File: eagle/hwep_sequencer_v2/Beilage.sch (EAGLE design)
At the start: 145 parts, among them X1 ESP32-DEVKIT-C

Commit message: final commit before testing
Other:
- note added: "Index/Cursor"
- note removed: "Select"
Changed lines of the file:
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@@
 <wire x1="5.08" y1="48.26" x2="5.08" y2="154.94" width="0.1524" layer="97" style="dashdot"/>
 <text x="93.98" y="261.62" size="1.778" layer="97" font="vector" align="bottom-center">Key Register Bar Interface</text>
-<text x="48.26" y="149.86" size="1.778" layer="97" font="vector" align="bottom-center">Select</text>
+<text x="48.26" y="149.86" size="1.778" layer="97" font="vector" align="bottom-center">Index/Cursor</text>
 <text x="142.24" y="149.86" size="1.778" layer="97" font="vector" align="bottom-center">Enable</text>
 <wire x1="83.82" y1="144.78" x2="83.82" y2="147.32" width="0.1524" layer="97"/>

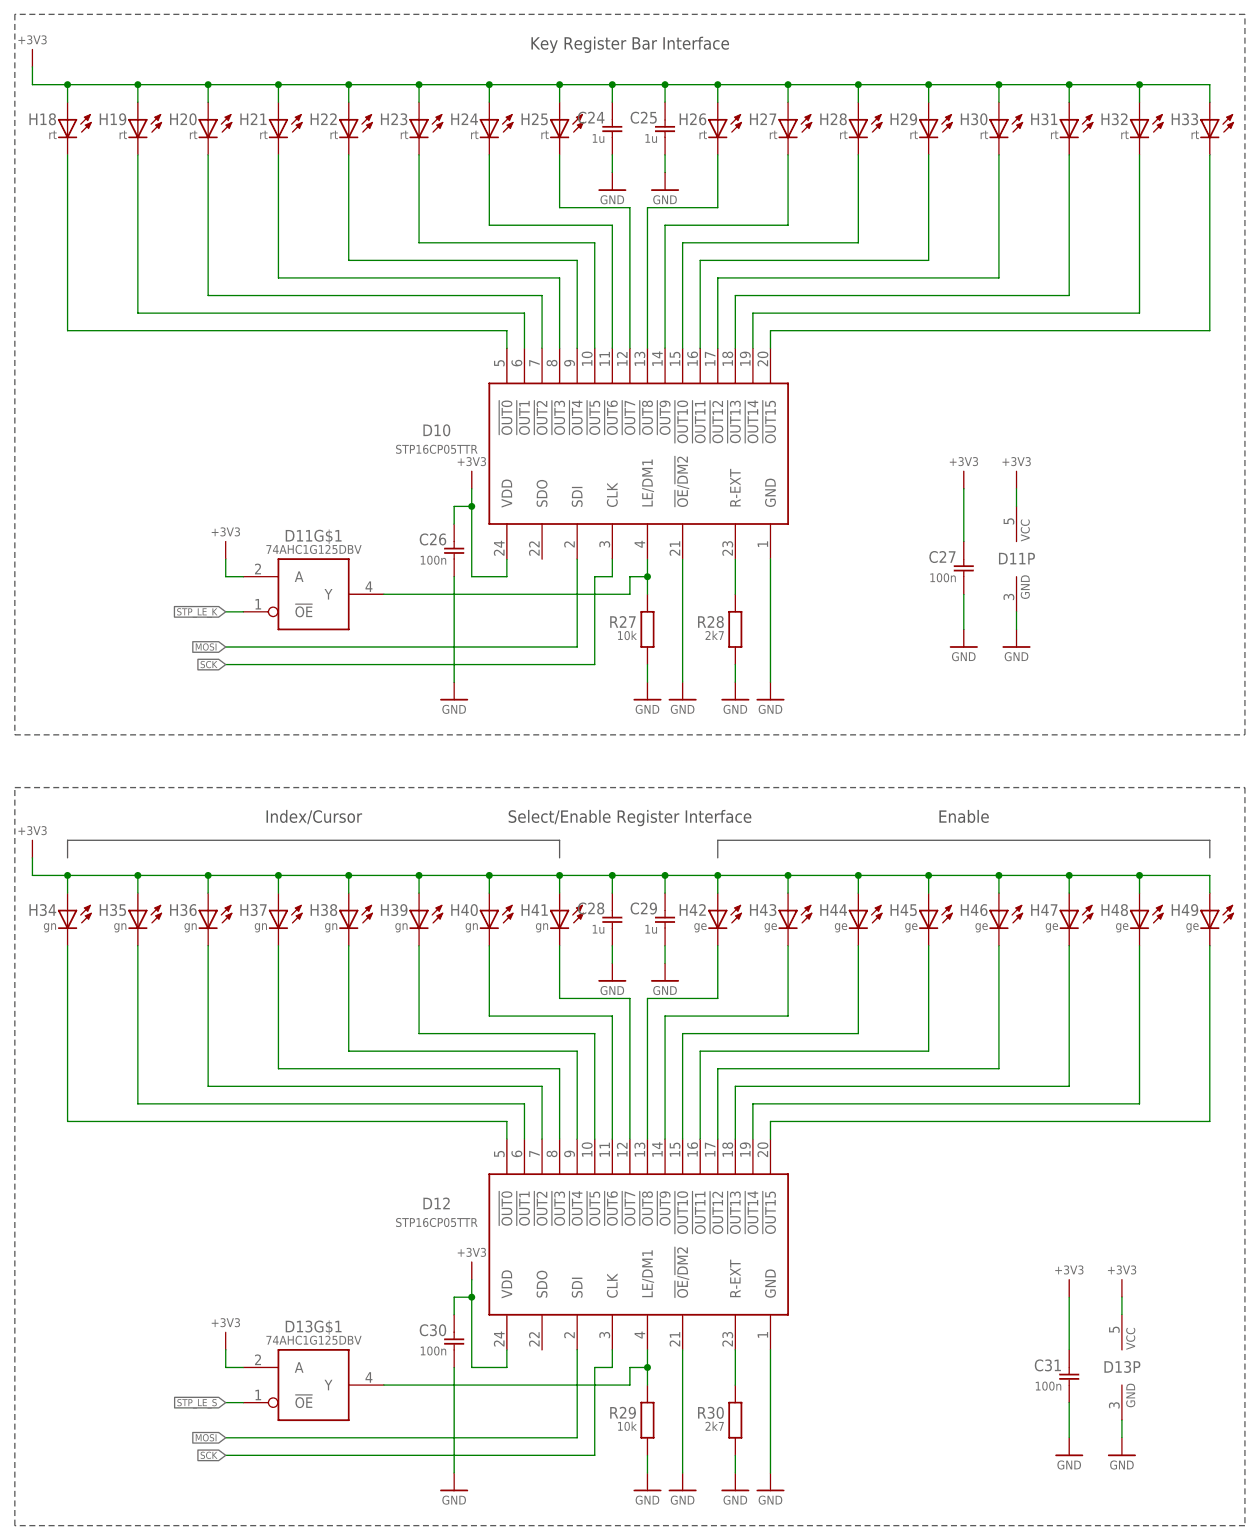
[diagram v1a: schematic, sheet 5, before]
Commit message: removed key register visualisation
bloat feature
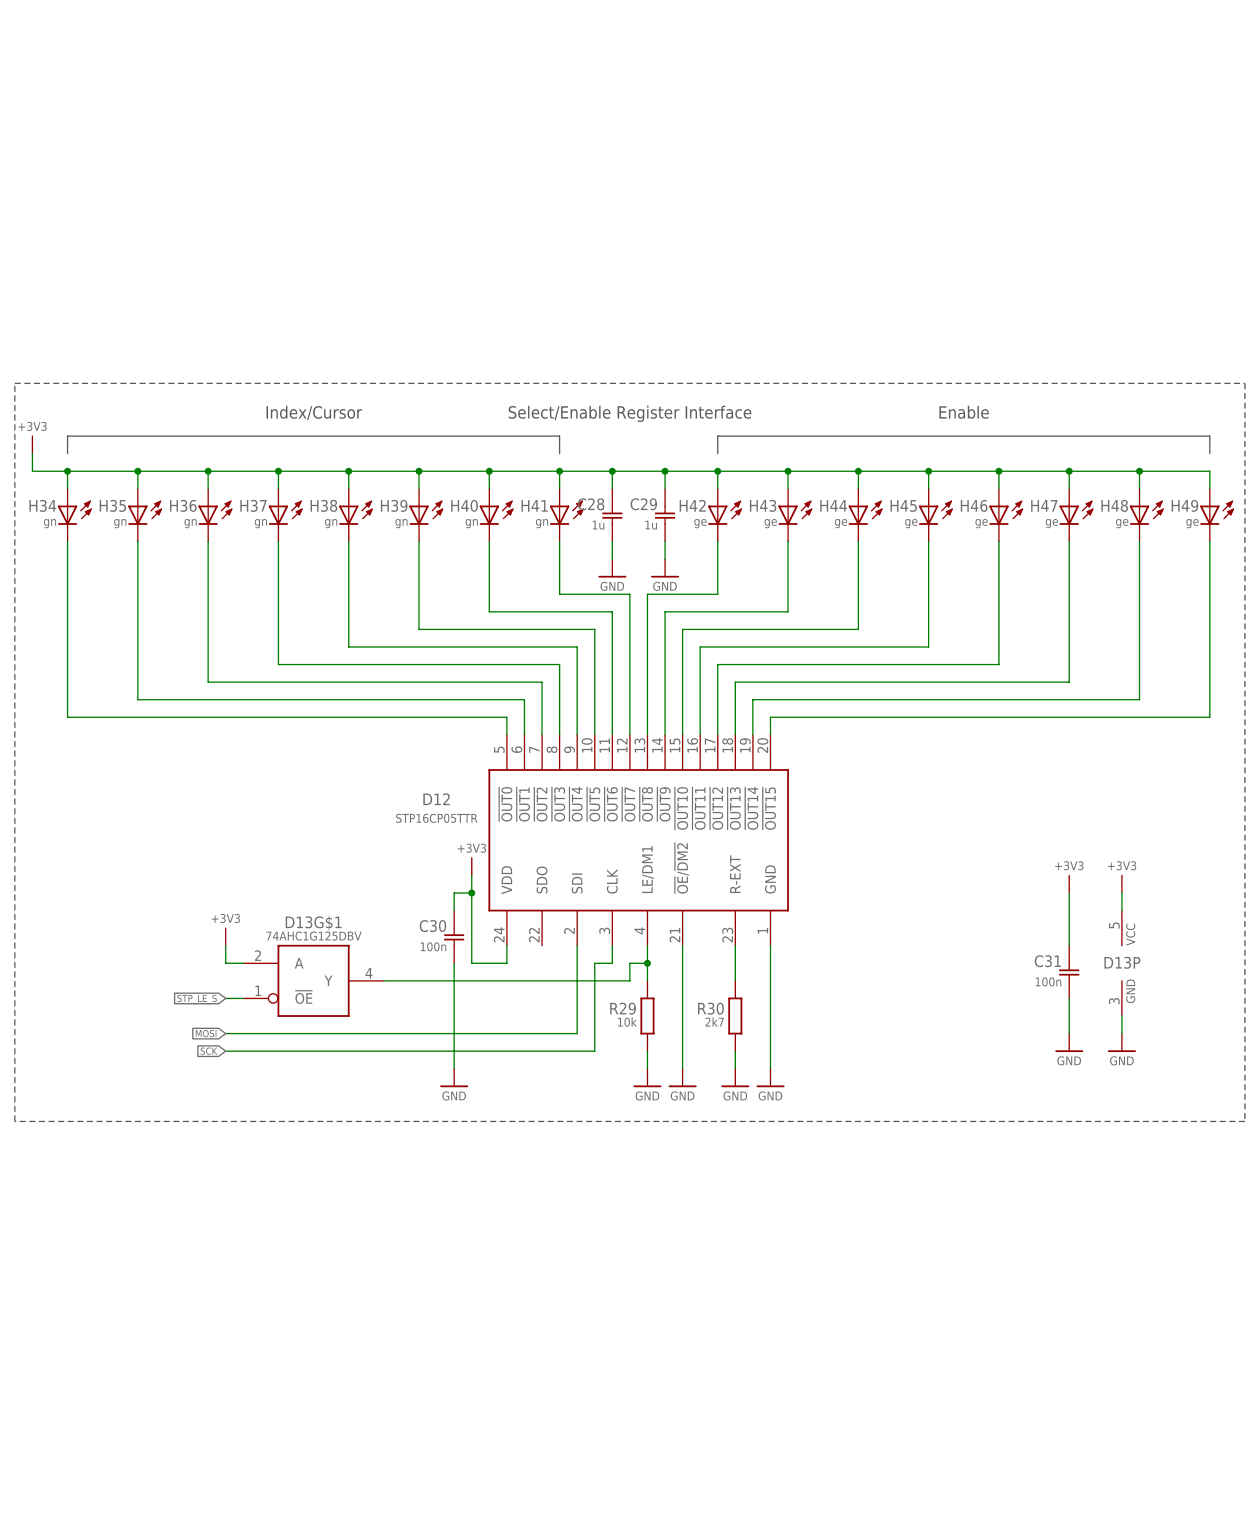
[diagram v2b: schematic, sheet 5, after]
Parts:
- removed C24, C25: 1u, rcl_GruS:C-EUC0805
- removed C26, C27: 100n, rcl_GruS:C-EUC0805
- removed D10: STP16CP05TTR, ic_GruS:STP16CP05TTR
- removed D11: 74AHC1G125DBV, 74xx_GruS:74AHC1G125DBV
- removed H18, H19, H20, H21, H22, H23, H24, H25, H26, H27, H28, H29, H30, H31, H32, H33: rt, led_GruS:LEDCHIPLED_1206
- removed R27: 10k, rcl_GruS:R-EUSR0805
- removed R28: 2k7, rcl_GruS:R-EUSR0805
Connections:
- net CLRR renamed RKR
- removed net N$10: D10.!OUT0, H18.C
- removed net N$11: D10.!OUT1, H19.C
- removed net N$12: D10.!OUT2, H20.C
- removed net N$13: D10.!OUT3, H21.C
- removed net N$20: D10.!OUT4, H22.C
- removed net N$21: D10.!OUT5, H23.C
- removed net N$22: D10.!OUT6, H24.C
- removed net N$23: D10.!OUT7, H25.C
- removed net N$24: D10.R-EXT, R28.2
- removed net N$25: D10.!OUT8, H26.C
- removed net N$26: D10.!OUT9, H27.C
- removed net N$27: D10.!OUT10, H28.C
- removed net N$28: D10.!OUT11, H29.C
- removed net N$29: D10.!OUT12, H30.C
- removed net N$30: D10.!OUT13, H31.C
- removed net N$31: D10.!OUT14, H32.C
- removed net N$32: D10.!OUT15, H33.C
- removed net N$66: D10.LE/DM1, D11G$1.Y, R27.2
- net +3V3: no longer C24.1, C25.1, C26.1, C27.1, D10.VDD, D11G$1.A, D11P.VCC, H18.A, H19.A, H20.A, H21.A, H22.A, H23.A, H24.A, H25.A, H26.A, H27.A, H28.A, H29.A, H30.A, H31.A, H32.A, H33.A
- net GND: no longer C24.2, C25.2, C26.2, C27.2, D10.!OE!/!DM2, D10.GND, D11P.GND, R27.1, R28.1
- net MOSI: no longer D10.SDI
- net SCK: no longer D10.CLK
- net STP_LE_K: no longer D11G$1.!OE
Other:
- note removed: "Key Register Bar Interface"
- moved on the sheet: C28, C29, C30, C31, D12, D13G$1, D13P, H34, H35, H36, H37, H38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

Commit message: upd doku
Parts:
- C4: CATEGORY (none) -> 2
- X3, X4: CATEGORY (none) -> 18
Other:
- note removed: "Prescaler 4-bit encoded data priority on BPM Divider Inputs"
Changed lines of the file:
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@@
 <attributes>
 <attribute name="ABTEILUNG" value="Technische Informatik"/>
-<attribute name="BEARBEITER" value="Simon Grundner"/>
-<attribute name="DATUM" value="2021//"/>
+<attribute name="BEARBEITER" value="Ihninger, Grundner"/>
+<attribute name="DATUM" value="07/02/2022"/>
 <attribute name="DOKUMENTART" value="Schaltplan"/>
 <attribute name="GEZ" value="GruS"/>
@@
 <part name="GND11" library="supply_GruS" library_urn="urn:adsk.eagle:library:13579815" deviceset="AGND" device=""/>
 <part name="GND12" library="supply_GruS" library_urn="urn:adsk.eagle:library:13579815" deviceset="AGND" device=""/>
-<part name="X4" library="con_GruS" library_urn="urn:adsk.eagle:library:13569504" deviceset="JUMPSMD1FACH-1" device="" package3d_urn="urn:adsk.eagle:package:33704775/1"/>
-<part name="X3" library="con_GruS" library_urn="urn:adsk.eagle:library:13569504" deviceset="JUMPSMD1FACH-1" device="" package3d_urn="urn:adsk.eagle:package:33704775/1"/>
+<part name="X4" library="con_GruS" library_urn="urn:adsk.eagle:library:13569504" deviceset="JUMPSMD1FACH-1" device="" package3d_urn="urn:adsk.eagle:package:33704775/1">
+<attribute name="CATEGORY" value="18"/>
+</part>
+<part name="X3" library="con_GruS" library_urn="urn:adsk.eagle:library:13569504" deviceset="JUMPSMD1FACH-1" device="" package3d_urn="urn:adsk.eagle:package:33704775/1">
+<attribute name="CATEGORY" value="18"/>
+</part>
 <part name="U$10" library="supply_GruS" library_urn="urn:adsk.eagle:library:13579815" deviceset="VREF" device=""/>
 <part name="+5V25" library="supply_GruS" library_urn="urn:adsk.eagle:library:13579815" deviceset="+5V" device=""/>
@@
 <part name="GND75" library="supply_GruS" library_urn="urn:adsk.eagle:library:13579815" deviceset="AGND" device=""/>
 <part name="U$11" library="supply_GruS" library_urn="urn:adsk.eagle:library:13579815" deviceset="VREF" device=""/>
-<part name="C4" library="rcl_GruS" library_urn="urn:adsk.eagle:library:13572313" deviceset="C-EU" device="C0805" package3d_urn="urn:adsk.eagle:package:23617/2" value="4u7"/>
+<part name="C4" library="rcl_GruS" library_urn="urn:adsk.eagle:library:13572313" deviceset="C-EU" device="C0805" package3d_urn="urn:adsk.eagle:package:23617/2" value="4u7">
+<attribute name="CATEGORY" value="2"/>
+</part>
 <part name="GND76" library="supply_GruS" library_urn="urn:adsk.eagle:library:13579815" deviceset="GND" device=""/>
 </parts>
@@
 <attribute name="NAME" x="24.13" y="116.078" size="1.6764" layer="95" rot="R180"/>
 <attribute name="VALUE" x="29.464" y="114.808" size="1.27" layer="96"/>
+<attribute name="CATEGORY" x="25.4" y="114.3" size="1.778" layer="96" display="off"/>
 </instance>
 <instance part="X3" gate="1" x="38.1" y="127" smashed="yes">
 <attribute name="NAME" x="34.29" y="128.778" size="1.6764" layer="95" rot="R180"/>
 <attribute name="VALUE" x="34.036" y="126.492" size="1.27" layer="96" rot="R180"/>
+<attribute name="CATEGORY" x="38.1" y="127" size="1.778" layer="96" display="off"/>
 </instance>
 <instance part="U$10" gate="G$1" x="22.86" y="129.54" smashed="yes" rot="MR0">
@@
 <attribute name="NAME" x="14.224" y="121.3866" size="1.6764" layer="95" font="vector" align="bottom-right"/>
 <attribute name="VALUE" x="14.224" y="118.5926" size="1.27" layer="96" font="vector" align="bottom-right"/>
+<attribute name="CATEGORY" x="15.24" y="121.92" size="1.778" layer="96" display="off"/>
 </instance>
 </instances>
@@
 <wire x1="25.4" y1="114.3" x2="25.4" y2="203.2" width="0.1524" layer="97" style="dashdot"/>
 <text x="93.98" y="198.12" size="1.778" layer="97" font="vector" align="bottom-center">Prescaler Input Encoder</text>
-<text x="25.4" y="208.28" size="1.778" layer="150">Prescaler
-4-bit encoded data
-priority on BPM Divider Inputs</text>
 </plain>
 <instances>

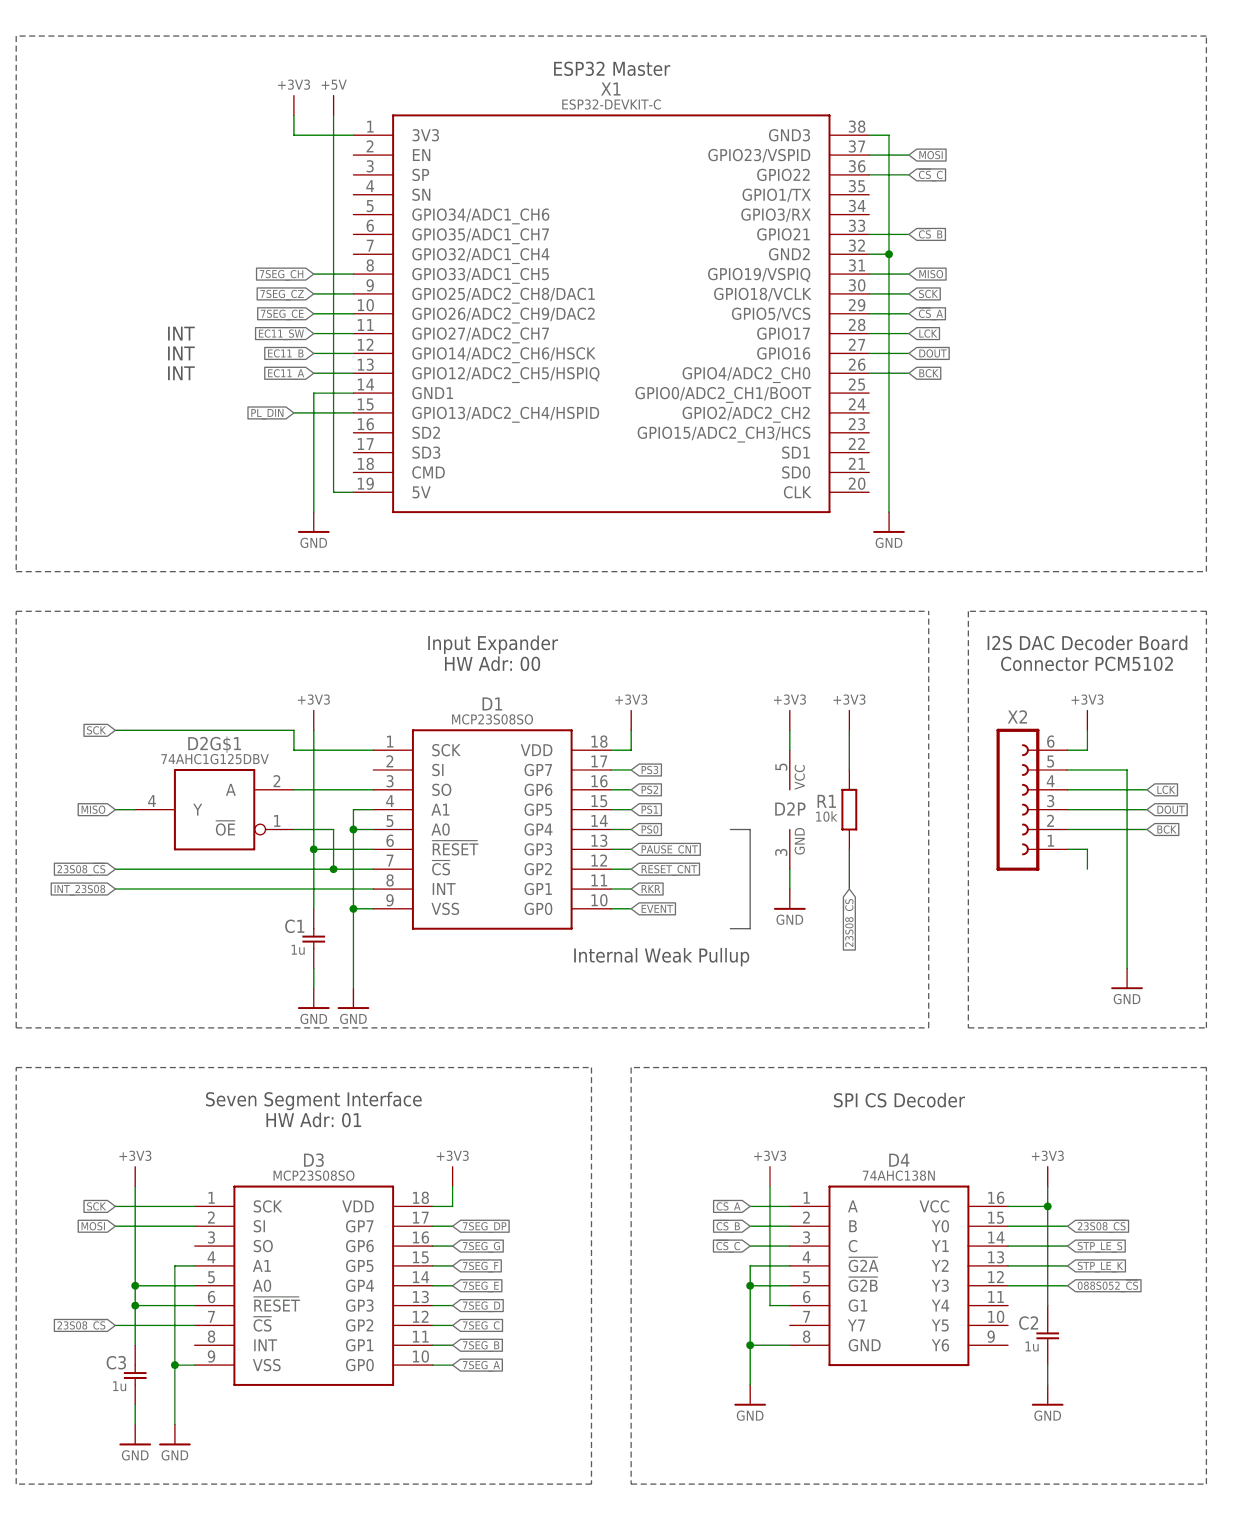
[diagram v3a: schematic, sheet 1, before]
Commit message: removed unnecessary features
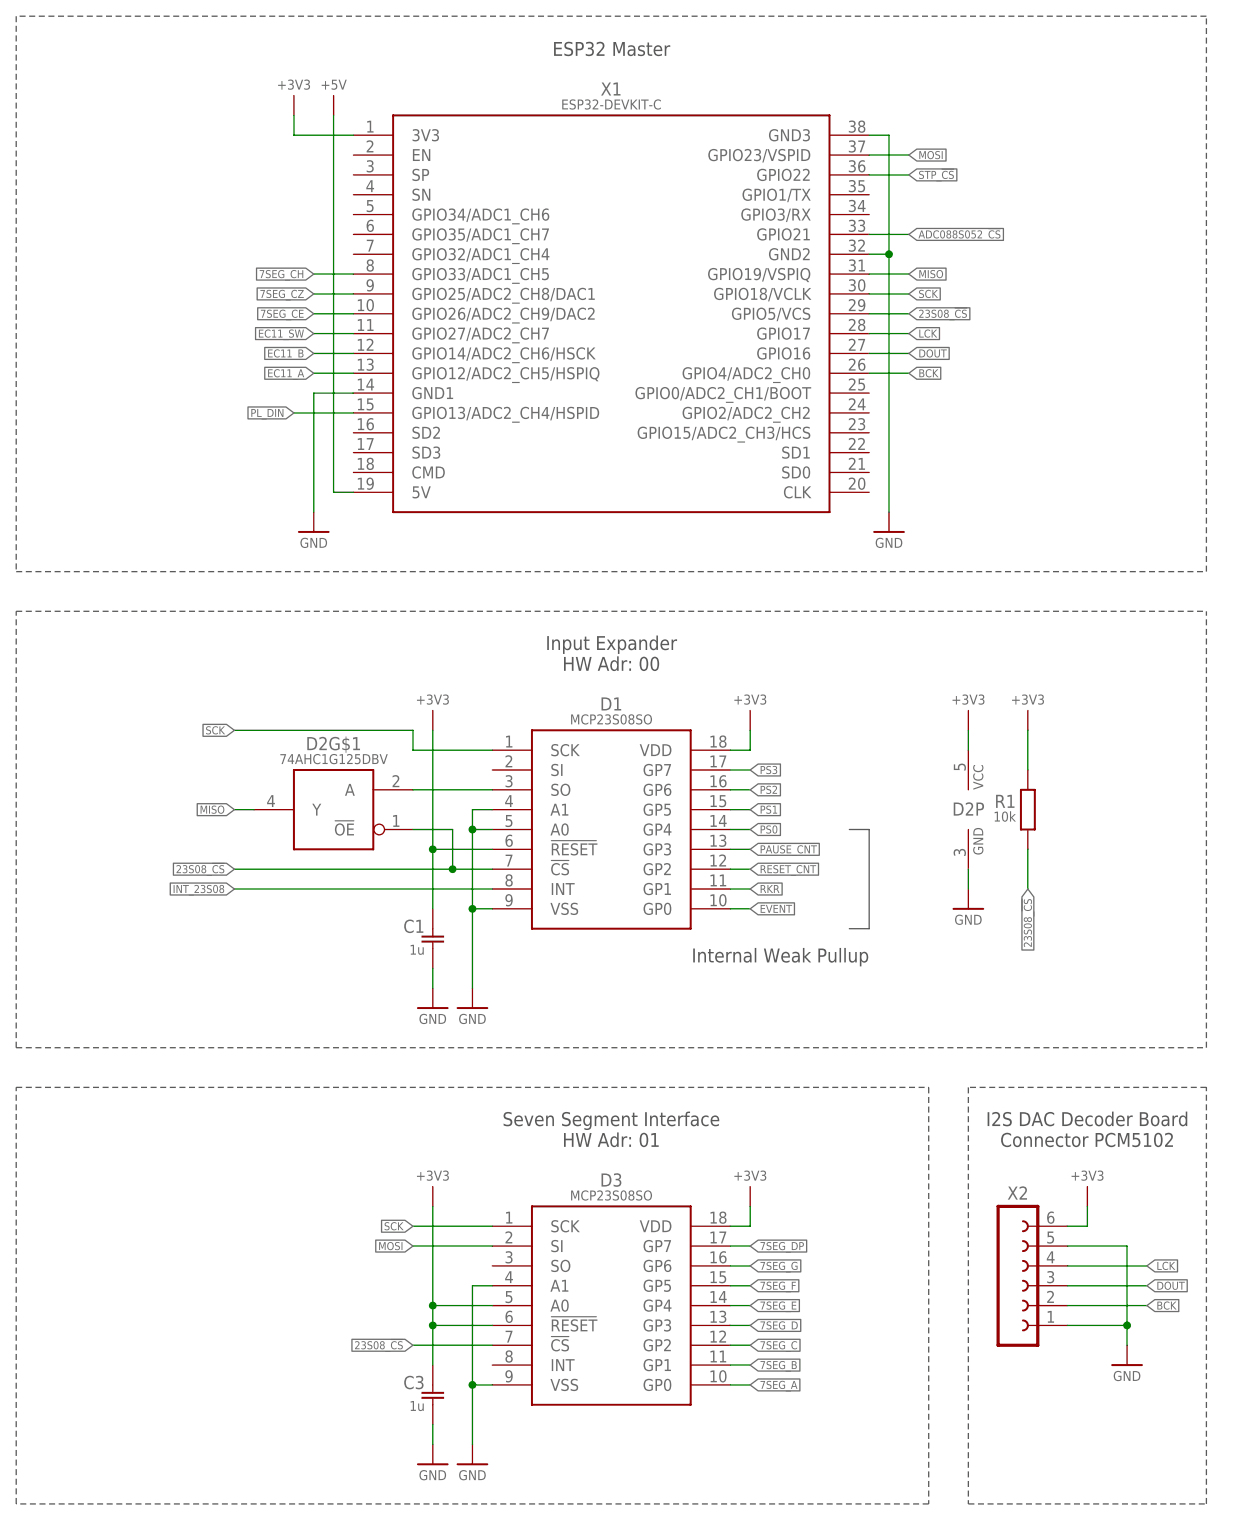
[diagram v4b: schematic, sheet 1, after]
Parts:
- removed C2: 1u, rcl_GruS:C-EUC0805
- removed D4: 74AHC138N, 74xx_GruS:74AHC138N
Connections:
- removed net !CS!_A: D4.A, X1.GPIO5/VCS
- removed net !CS!_B: D4.B, X1.GPIO21
- removed net !CS!_C: D4.C, X1.GPIO22
- removed net 088S052_!CS!: D4.Y3, D5.!CS, R15.1
- removed net N$1: X2.1
- removed net STP_LE_K: D4.Y2
- removed net STP_LE_S: D13G$1.!OE, D4.Y1
- new net ADC088S052_!CS: D5.!CS, R15.1, X1.GPIO21
- new net STP_!CS: D13G$1.!OE, X1.GPIO22
- net +3V3: no longer C2.1, D4.G1, D4.VCC
- net 23S08_!CS: now also X1.GPIO5/VCS; no longer D4.Y0
- net GND: now also X2.1; no longer C2.2, D4.!G2A, D4.!G2B, D4.GND
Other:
- note removed: "INT"
- note removed: "SPI CS Decoder"
- moved on the sheet: C1, C3, C30, C31, D1, D13G$1, D13P, D2G$1, D2P, D3, R1, R29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
